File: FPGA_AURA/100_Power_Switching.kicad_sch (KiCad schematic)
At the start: 6 parts, among them J1 USB_C_Receptacle_USB2.0_16P, U1 XC7A35T-2FTG256C

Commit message: Initial component selection done
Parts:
- added J101: XT30PW-M, XT30PWM:XT30PWM, symbol XT30PW-M:XT30PW-M
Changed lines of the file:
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@@
+	)
+	(symbol
+		(lib_id "XT30PW-M:XT30PW-M")
+		(at 46.99 119.38 0)
+		(unit 1)
+		(exclude_from_sim no)
+		(in_bom yes)
+		(on_board yes)
+		(dnp no)
+		(fields_autoplaced yes)
+		(property "Reference" "J101"
+			(at 57.15 111.76 0)
+			(effects
+				(font
+					(size 1.27 1.27)
+				)
+			)
+		)
+		(property "Value" "XT30PW-M"
+			(at 57.15 114.3 0)
+			(effects
+				(font
+					(size 1.27 1.27)
+				)
+			)
+		)
+		(property "Footprint" "XT30PWM:XT30PWM"
+			(at 63.5 214.3 0)
+			(effects
+				(font
+					(size 1.27 1.27)
+				)
+				(justify left top)
+				(hide yes)
+			)
+		)
+		(property "Datasheet" "https://www.tme.eu/sl/Document/ce4077e36b79046da520ca73227e15de/XT30PW%20SPEC.pdf"
+			(at 63.5 314.3 0)
+			(effects
+				(font
+					(size 1.27 1.27)
+				)
+				(justify left top)
+				(hide yes)
+			)
+		)
+		(property "Description" "30A Low Temperature Rise Fire Retardant Plug"
+			(at 46.99 119.38 0)
+			(effects
+				(font
+					(size 1.27 1.27)
+				)
+				(hide yes)
+			)
+		)
+		(property "Height" "5"
+			(at 63.5 514.3 0)
+			(effects
+				(font
+					(size 1.27 1.27)
+				)
+				(justify left top)
+				(hide yes)
+			)
+		)
+		(property "Manufacturer_Name" "Amass"
+			(at 63.5 614.3 0)
+			(effects
+				(font
+					(size 1.27 1.27)
+				)
+				(justify left top)
+				(hide yes)
+			)
+		)
+		(property "Manufacturer_Part_Number" "XT30PW-M"
+			(at 63.5 714.3 0)
+			(effects
+				(font
+					(size 1.27 1.27)
+				)
+				(justify left top)
+				(hide yes)
+			)
+		)
+		(property "Mouser Part Number" ""
+			(at 63.5 814.3 0)
+			(effects
+				(font
+					(size 1.27 1.27)
+				)
+				(justify left top)
+				(hide yes)
+			)
+		)
+		(property "Mouser Price/Stock" ""
+			(at 63.5 914.3 0)
+			(effects
+				(font
+					(size 1.27 1.27)
+				)
+				(justify left top)
+				(hide yes)
+			)
+		)
+		(property "Arrow Part Number" ""
+			(at 63.5 1014.3 0)
+			(effects
+				(font
+					(size 1.27 1.27)
+				)
+				(justify left top)
+				(hide yes)
+			)
+		)
+		(property "Arrow Price/Stock" ""
+			(at 63.5 1114.3 0)
+			(effects
+				(font
+					(size 1.27 1.27)
+				)
+				(justify left top)
+				(hide yes)
+			)
+		)
+		(pin "1"
+		)
+		(pin "2"
+		)
+		(pin "4"
+		)
+		(pin "3"
+		)
+		(instances
+			(project ""
+				(path "/3d83cb23-9528-4d06-8969-599520e9eb23/ce047a46-50f2-4465-991d-ae0222187798"
+					(reference "J101")
+					(unit 1)
+				)
+			)
+		)
 	)
 	(symbol

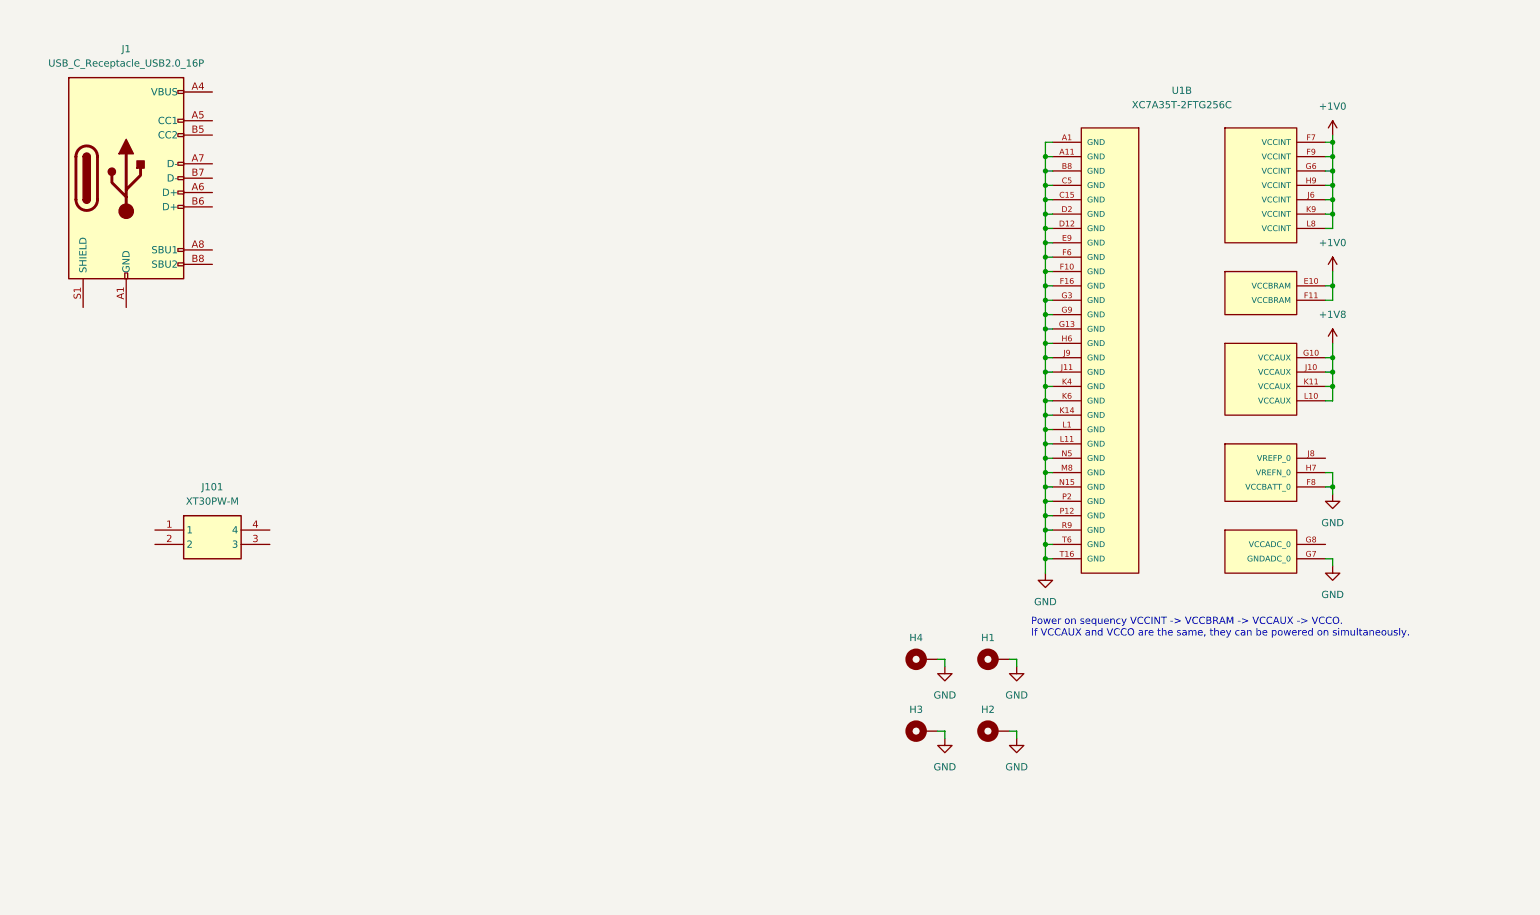
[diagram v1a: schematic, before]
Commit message: Added USB power schottky and started DDR3L
Transferring from laptop to PC to decide DDR3 pins.
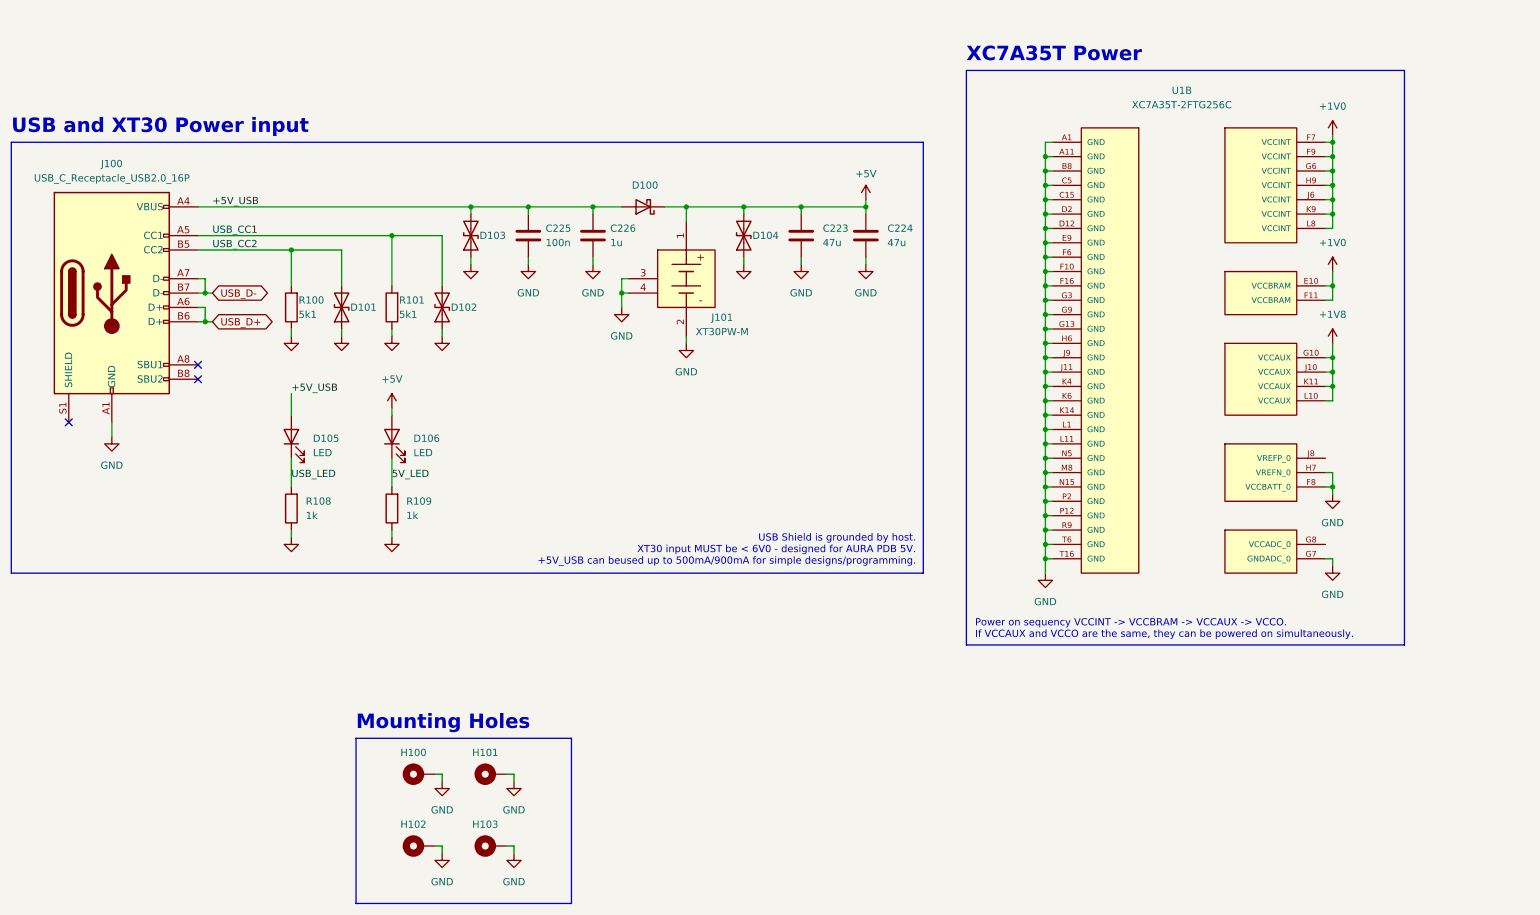
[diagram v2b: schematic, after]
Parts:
- added C223, C224: 47u, Capacitor_SMD:C_0805_2012Metric, symbol Device:C
- added C225: 100n, Capacitor_SMD:C_0402_1005Metric, symbol Device:C
- added C226: 1u, Capacitor_SMD:C_0402_1005Metric, symbol Device:C
- added D100: D_Schottky, symbol Device:D_Schottky
- added D101, D102, D103, D104: D_TVS, symbol Device:D_TVS
- added D105, D106: LED, LED_SMD:LED_0603_1608Metric, symbol Device:LED
- added R100, R101: 5k1, Resistor_SMD:R_0402_1005Metric, symbol Device:R
- added R108, R109: 1k, Resistor_SMD:R_0402_1005Metric, symbol Device:R
- renumbered H4 to H100, H1 to H101, H3 to H102, H2 to H103, J1 to J100
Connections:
- net GND: now also J100.A1 (GND), J100.A12 (GND), J100.B1 (GND), J100.B12 (GND), J101.2, J101.3, J101.4, C223.2, C224.2, C225.2, C226.2, D101.1 (A1), D102.1 (A1), D103.1 (A1), D104.1 (A1), R100.1, R101.1, R108.1, R109.1
- net +5V_USB: now reaches J100.A4 (VBUS), J100.A9 (VBUS), J100.B4 (VBUS), J100.B9 (VBUS)
- net +5V_USB: now also C225.1, C226.1, D100.2 (A), D103.2 (A2), D105.2 (A)
- net USB_CC1: now reaches J100.A5 (CC1)
- net USB_CC1: now also D102.2 (A2), R101.2
- net USB_D+: now reaches J100.A6 (D+)
- net USB_D+: now also J100.B6 (D+)
- net USB_D-: now reaches J100.A7 (D-)
- net USB_D-: now also J100.B7 (D-)
- net USB_CC2: now reaches J100.B5 (CC2)
- net USB_CC2: now also D101.2 (A2), R100.2
- net +5V: now reaches J101.1
- net +5V: now also C223.1, C224.1, D100.1 (K), D104.2 (A2), D106.2 (A)
- new net 5V_LED: D106.1 (K), R109.2
- new net USB_LED: D105.1 (K), R108.2
- no-connect marks 0 -> 3
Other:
- note added: "Mounting Holes"
- note added: "USB Shield is grounded by host. XT30 input MUST be < 6V0 - designed for AURA PDB 5V. +5V_USB can beused up to 500mA/900mA for simple designs/programming."
- note added: "USB and XT30 Power input"
- note added: "XC7A35T Power"
- moved on the sheet: H100, H101, H102, H103, J100

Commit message: Added Connectors, FPGA Power and organized sheets.
All schematic sheets now go up in order with the correct prefix.
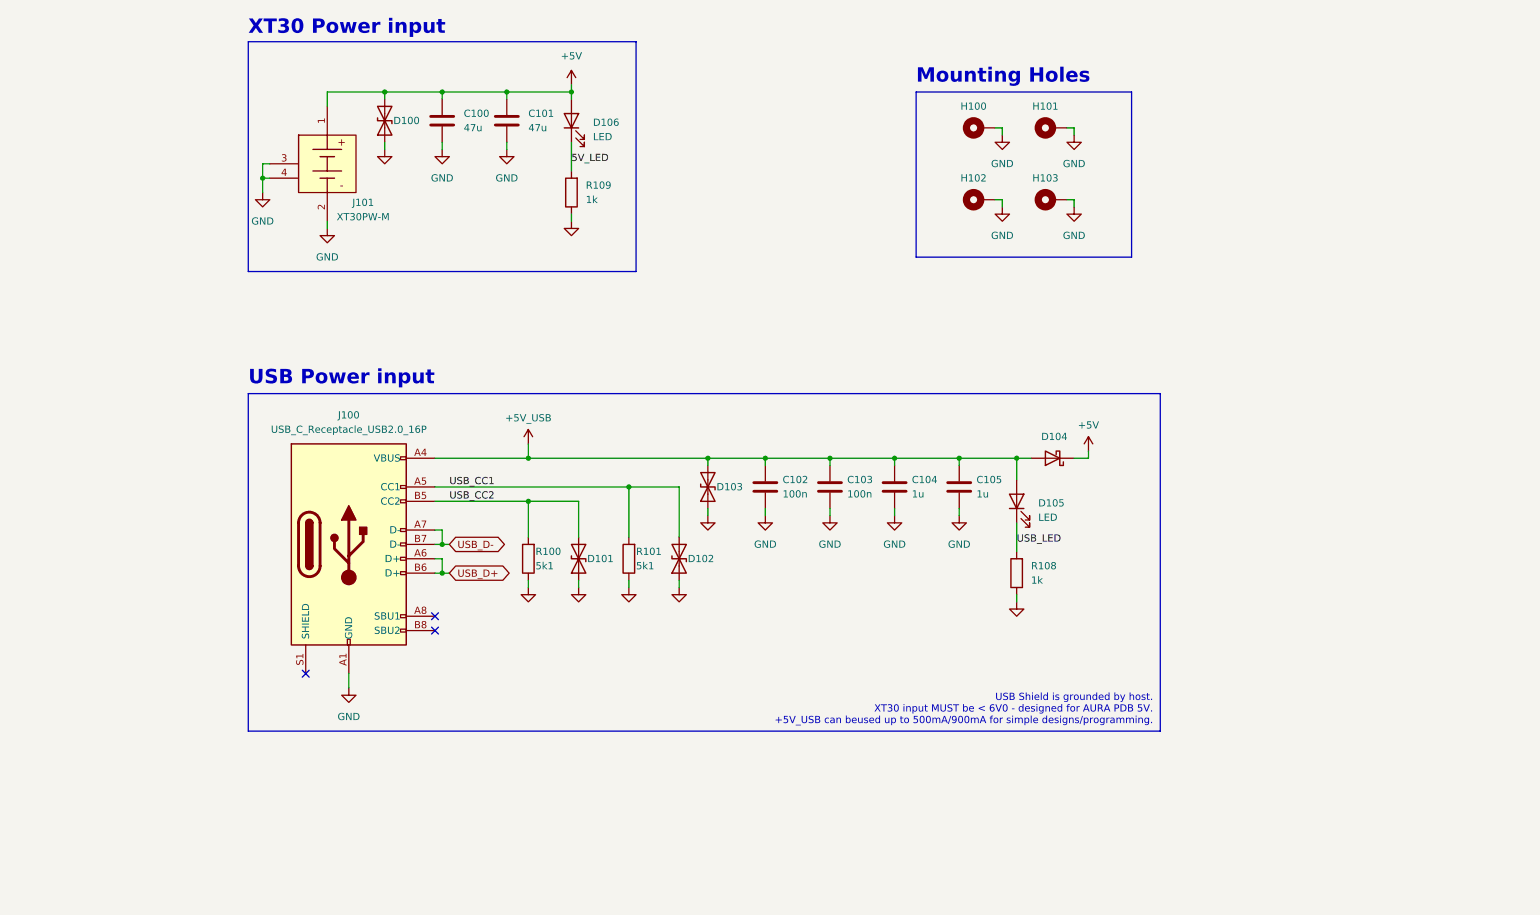
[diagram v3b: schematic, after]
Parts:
- removed U1: XC7A35T-2FTG256C, XC7A35T-2FTG256C:BGA256C100P16X16_1700X1700X155, symbol XC7A35T-2FTG256C:XC7A35T-2FTG256C
- added C103: 100n, Capacitor_SMD:C_0402_1005Metric, symbol Device:C
- added C105: 1u, Capacitor_SMD:C_0402_1005Metric, symbol Device:C
- renumbered C223 to C100, C224 to C101, C225 to C102, C226 to C104, D104 to D100, D100 to D104
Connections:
- net +5V_USB: now also C103.1, C105.1
- net GND: now also C103.2, C105.2
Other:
- note added: "USB Power input"
- note added: "XT30 Power input"
- note removed: "Power on sequency VCCINT -> VCCBRAM -> VCCAUX -> VCCO. If VCCAUX and VCCO are the same, they can be powered on simultaneously."
- note removed: "USB and XT30 Power input"
- note removed: "XC7A35T Power"
- moved on the sheet: C100, C101, C102, C104, D100, D101, D102, D103, D104, D105, D106, H100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
